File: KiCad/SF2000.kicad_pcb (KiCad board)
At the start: 4 copper layers, 111.5 x 83.9 mm, 76 parts, among them J1 Conn_2Rows-86Pins_even_odd, J10 Conn_02x01, J2 Conn_01x02, J3 Conn_02x03_Odd_Even, J4 Conn_02x01, J5 IDE_ATA_44pin, J6 Micro_SD_Card_Socket, J8 Conn_02x01, J9 Conn_02x01, U1 LM1117-3.3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

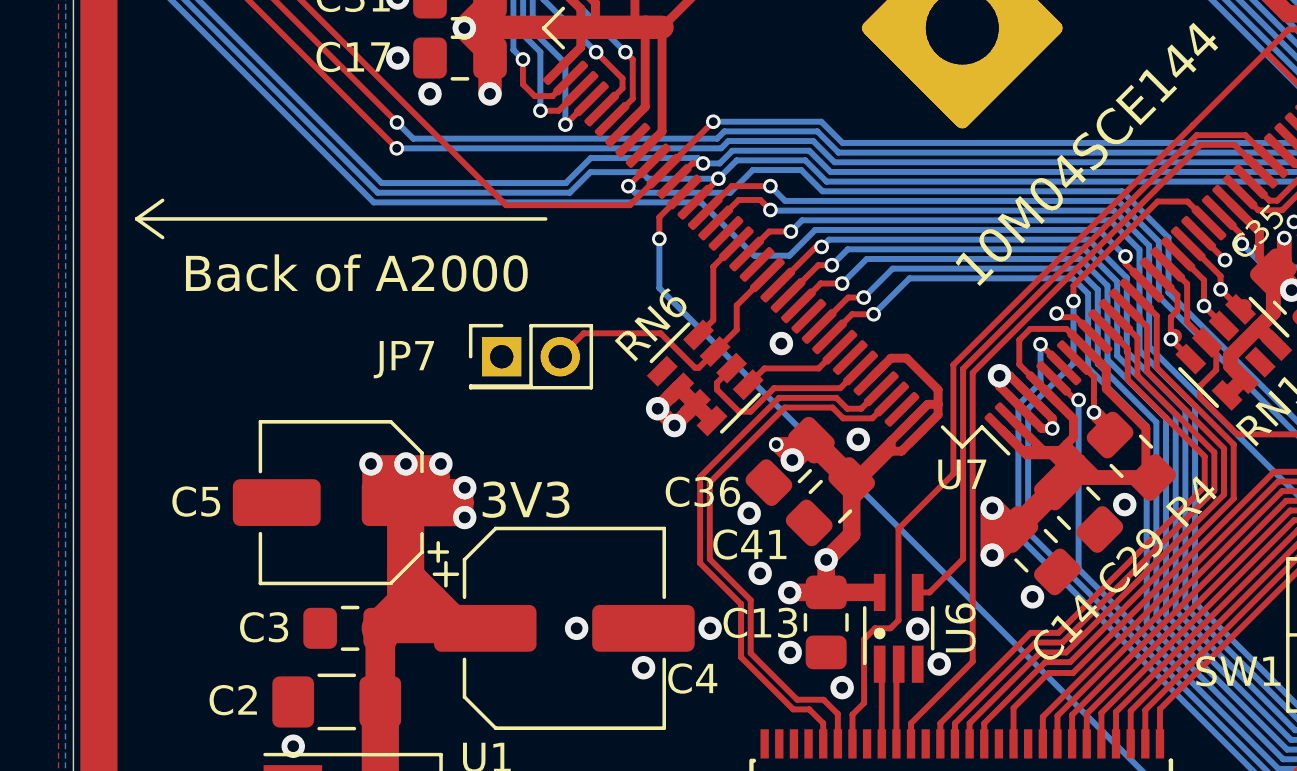
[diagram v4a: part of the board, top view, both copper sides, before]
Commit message: added capacitor for FPGA VCC-pin 128
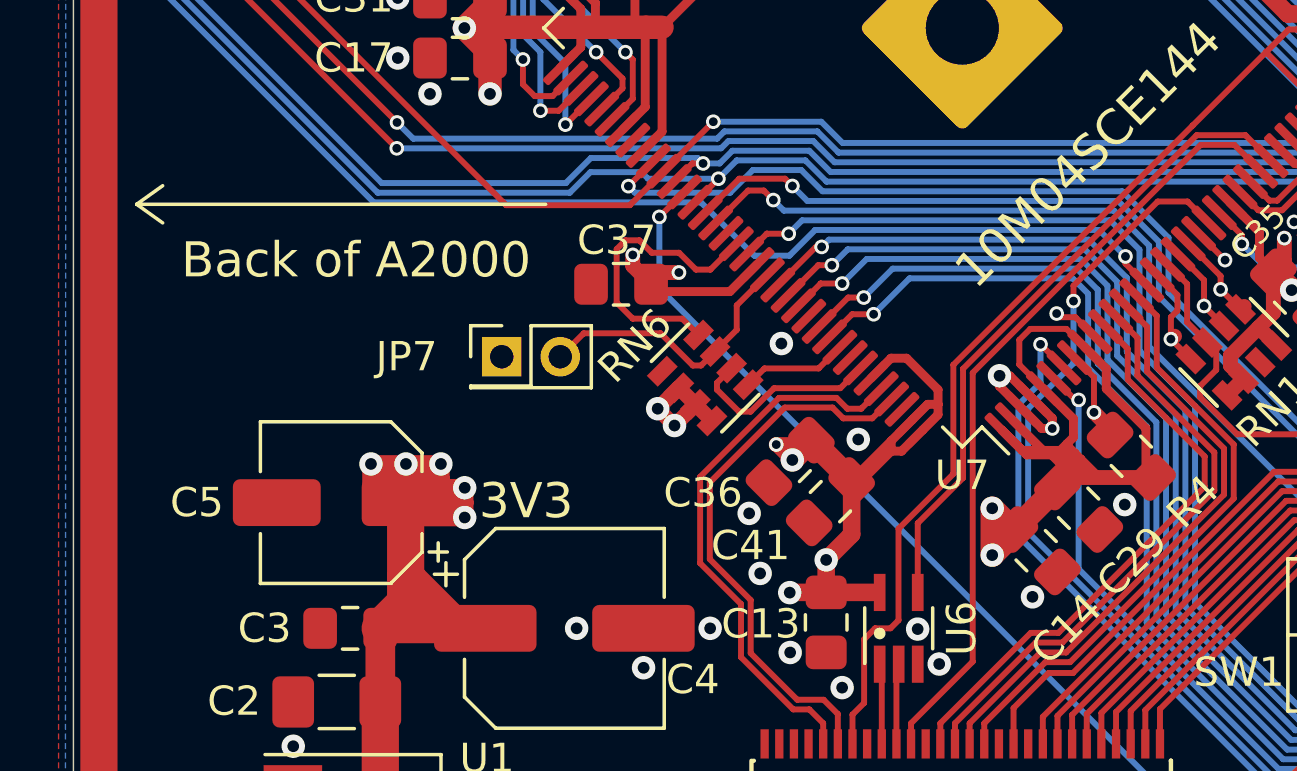
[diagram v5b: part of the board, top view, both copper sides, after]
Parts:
- added C37: 0.01uF, Capacitor_SMD:C_0805_2012Metric_Pad1.15x1.40mm_HandSolder, F.Cu at (116.4, 101.3)
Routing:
- net 3V3: track 313.5 -> 320.1 mm, vias 49 -> 51
- net CONFIG_SEL: track 3.65 -> 10.1 mm

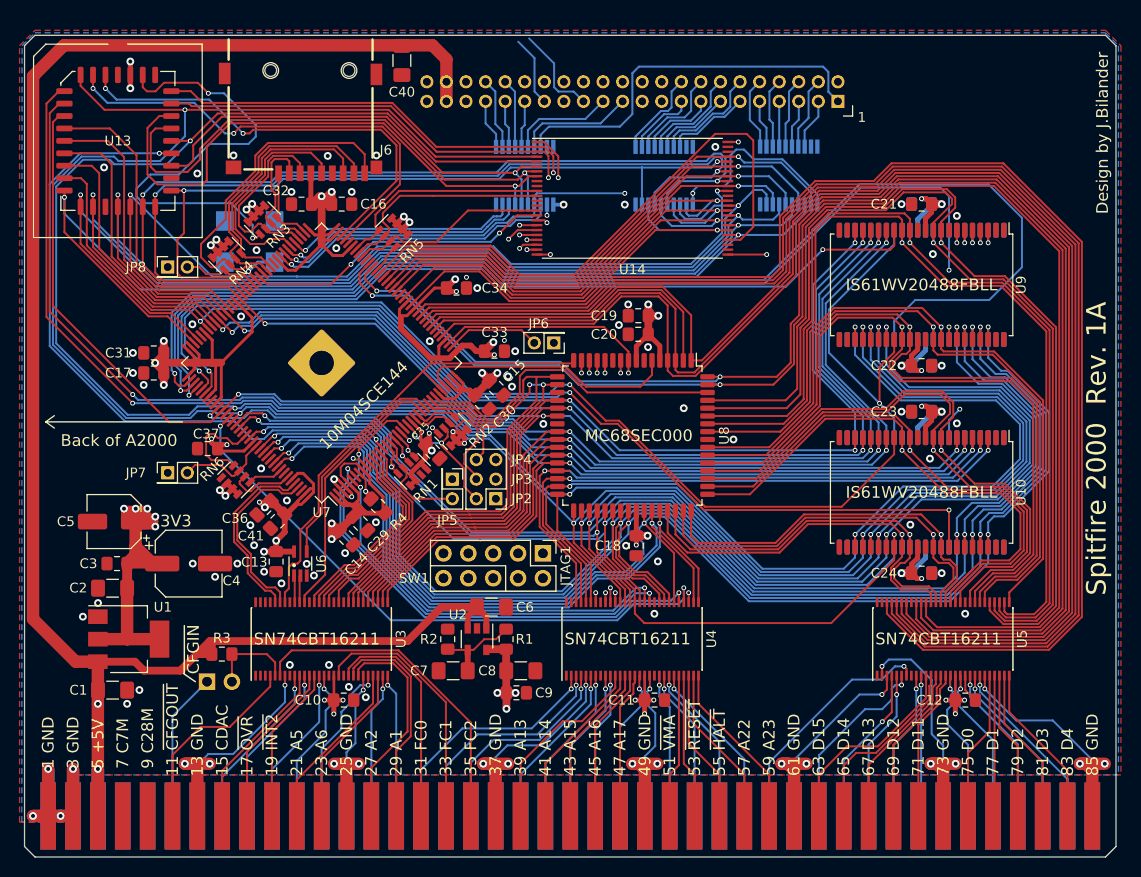
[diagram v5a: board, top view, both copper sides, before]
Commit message: added decoupling capacitors for IDE-buffers and ROM-chip
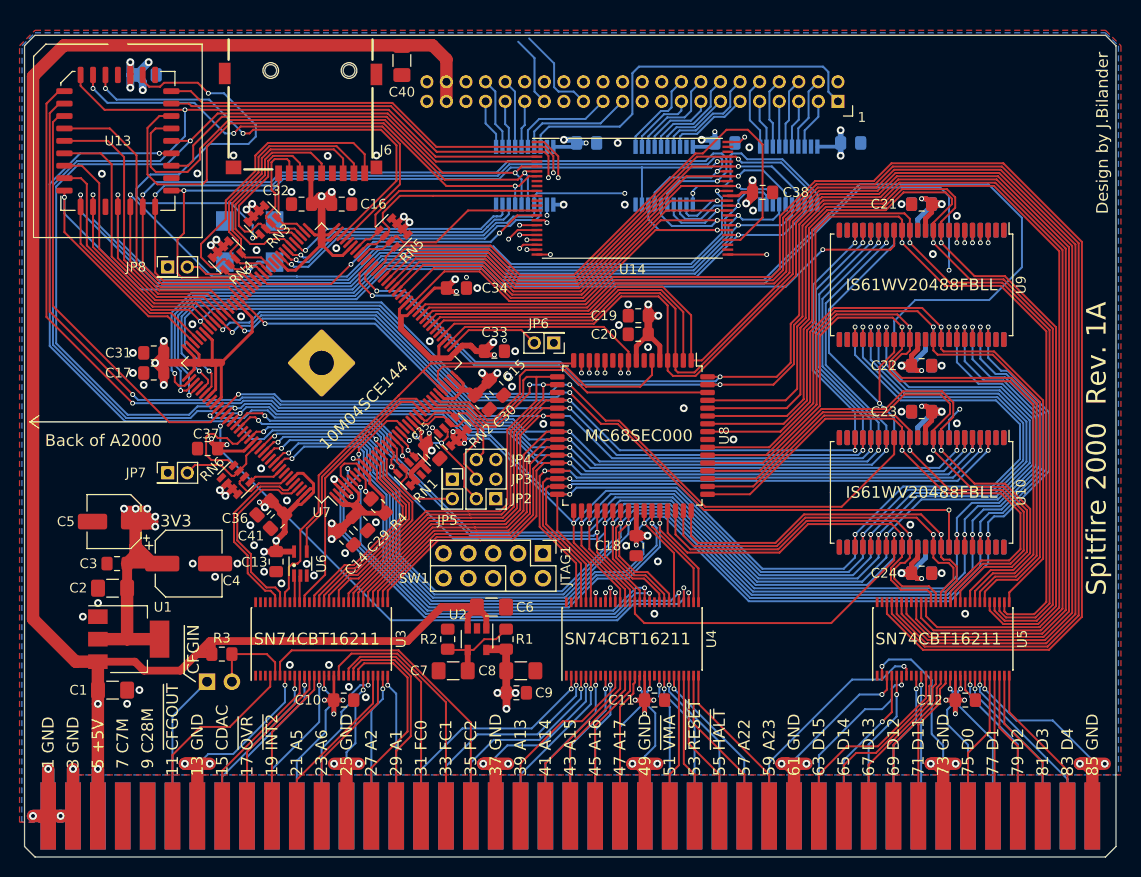
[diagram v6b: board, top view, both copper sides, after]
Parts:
- added C38: 0.01uF, Capacitor_SMD:C_0805_2012Metric_Pad1.15x1.40mm_HandSolder, F.Cu at (173.1, 75.2)
- added C42: 0.1uF, Capacitor_SMD:C_0805_2012Metric_Pad1.15x1.40mm_HandSolder, B.Cu at (110.1, 63.2)
- added C43: 0.1uF, Capacitor_SMD:C_0805_2012Metric_Pad1.15x1.40mm_HandSolder, B.Cu at (182.1, 70.1)
- added C44: 0.1uF, Capacitor_SMD:C_0805_2012Metric_Pad1.15x1.40mm_HandSolder, B.Cu at (169.2, 70.1)
- added C45: 0.1uF, Capacitor_SMD:C_0805_2012Metric_Pad1.15x1.40mm_HandSolder, B.Cu at (155.1, 70.1)
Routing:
- net 3V3: track 320.1 -> 347.3 mm, vias 51 -> 61
- net FLASH_OE: track 59.3 -> 60.7 mm
- net ROM_WE: track 75.8 -> 75.0 mm
- net D14_3V3: track 145.9 -> 146.6 mm
- net A2_3V3: track 182.7 -> 182.1 mm
- net D15_3V3: track 147.3 -> 147.8 mm
- net GND: vias 83 -> 85

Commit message: added decoupling capacitor for Crystal Oscillator (X1), and some silkcreen fixes/labeling
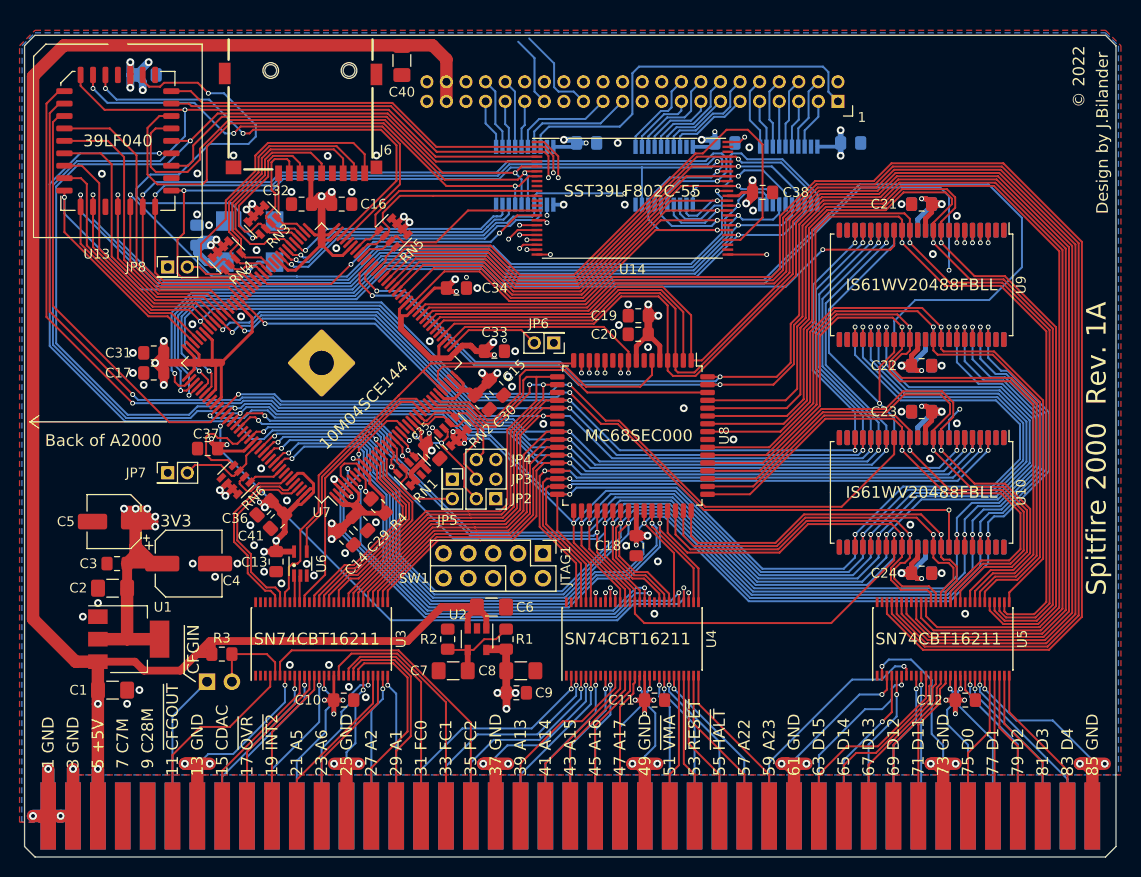
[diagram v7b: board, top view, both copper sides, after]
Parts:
- added C39: 0.01uF, Capacitor_SMD:C_0805_2012Metric_Pad1.15x1.40mm_HandSolder, B.Cu at (115.3, 79.5)
- renumbered U17 to U16, U16 to U17
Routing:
- net 3V3: track 347.3 -> 354.9 mm
- net GND: vias 85 -> 87
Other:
- board text added: "39LF040"
- board text added: "74LVC245"
- board text added: "SST39LF802C-55"
- board text added: "© 2022"
